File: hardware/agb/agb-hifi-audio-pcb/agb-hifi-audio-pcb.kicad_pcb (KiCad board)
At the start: 4 copper layers, 28.5 x 35.1 mm, 72 parts, among them J1 TC2030-IDC-NL, J5 SPK+, J6 SPK-, J7 EXPANSION0, J8 EXPANSION1, U1 ESP32-PICO-MINI-02-N8R2, U2 ES8388, U3 TPS61021ADSGR, U4 PAM8302AASCR, U5 LP5907MFX-3.0

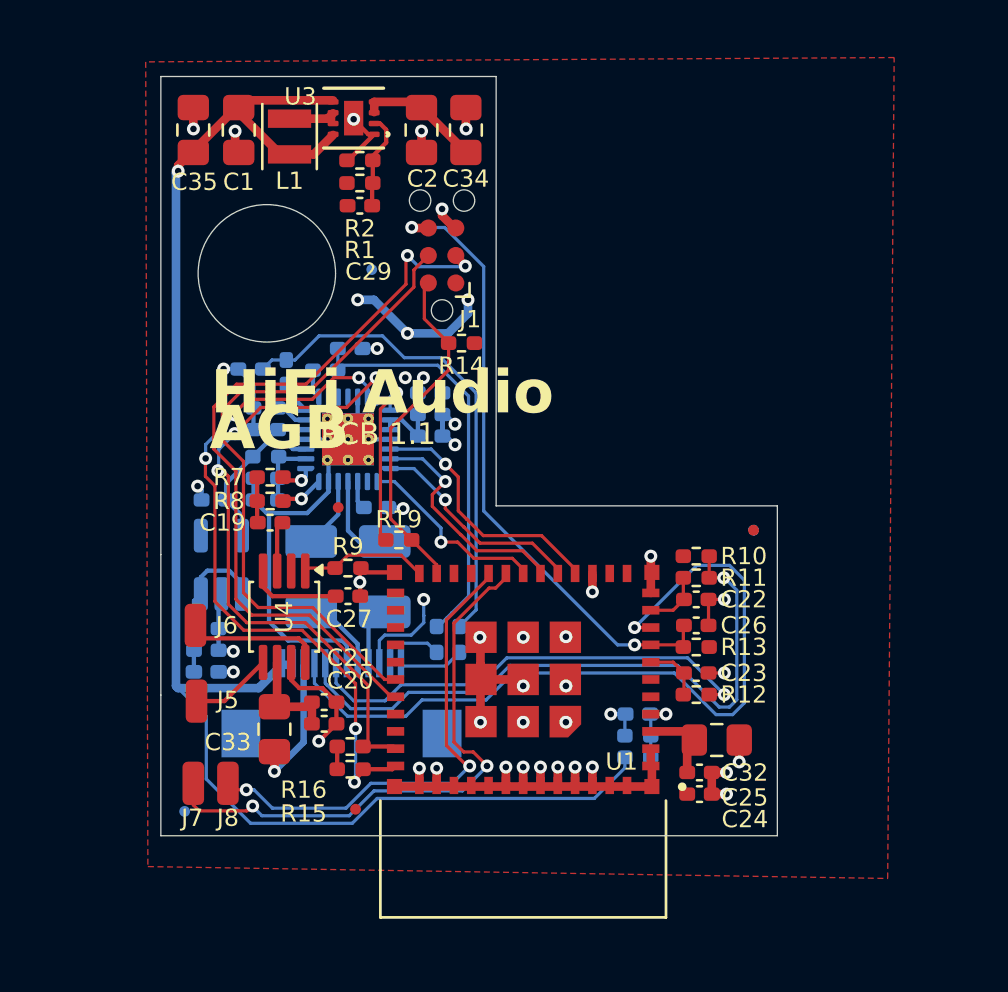
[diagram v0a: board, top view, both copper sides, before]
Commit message: hardware(agb): reroute mod PCB for the smaller shell fit; trim + reinforce FPC lead
Mod PCB: full reroute after narrowing the outline 28.5mm -> 25.35mm to fit the
shell. U2 (codec) moved and rotated 90deg with NT1 following; fiducials dropped
(sub-70x70 boards ride JLCPCB rails, which carry their own). Layout review
verified clean: DRC 0 unconnected, antenna keep-outs intact with the module
antenna overhanging the edge, zones refilled, power widths unchanged.

FPC: lead tip trimmed 1.25mm (y128 -> y126.75) to clear the volume wheel --
1.6mm is the geometric max without moving the J5 finger pattern, and the
shorter setback lands closer to the Hirose copper-to-tip recommendation.
Stiffener pulled flush with the new tip (4.85mm coverage vs 4.5mm minimum).
R2.0 fillets on both lead-base corners so the base stops tearing. Per-pad
0.15mm clearance overrides on the 12-pos connector pads.
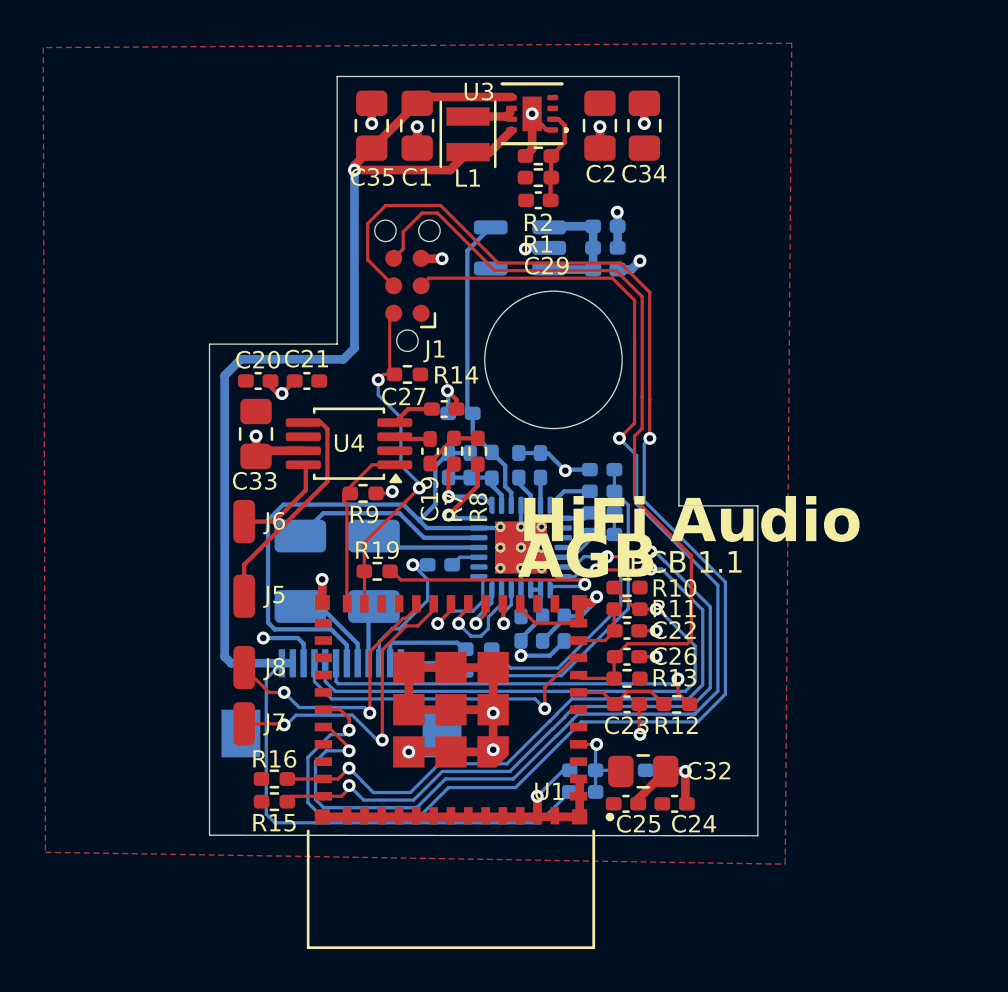
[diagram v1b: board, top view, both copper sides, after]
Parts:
- removed FID4 (x5), FID6: Fiducial_0.5mm_Mask1mm, Fiducial:Fiducial_0.5mm_Mask1mm
- moved C6 26.2 mm to (109.2, 98.2)
- moved C7 26.2 mm to (109.2, 99.2)
- moved FB1 26.2 mm to (109.2, 100.2)
- moved U5 20.1 mm to (105.2, 99.2), turned to 180 degrees
- moved C13 16.9 mm to (109.0, 109.5)
- moved C20 16.1 mm to (93.2, 105.4)
- moved C15 15.6 mm to (109.0, 110.5), turned to 180 degrees
- moved C21 14.9 mm to (95.4, 105.4), turned to 180 degrees
- moved C14 14.5 mm to (109.0, 112.5), turned to 180 degrees
- moved C16 14.4 mm to (109.0, 111.5)
- moved C33 13.7 mm to (93.0, 107.8)
- moved C12 13.0 mm to (106.2, 109.3), turned to 90 degrees
- moved C5 12.5 mm to (107.3, 116.8), turned to 90 degrees
- moved C31 12.1 mm to (102.5, 106.9)
- moved C11 11.8 mm to (105.2, 109.3), turned to 90 degrees
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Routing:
- net UART_RX: track 30.5 -> 66.9 mm, vias 0 -> 2
- net UART_TX: track 34.5 -> 56.7 mm
- net PAIR: track 36.2 -> 14.9 mm
- net +3V3: track 26.7 -> 7.27 mm, vias 5 -> 2
- net EXP0: track 26.8 -> 14.4 mm
- net EXP1: track 22.1 -> 12.5 mm
- net ESP_EN: track 28.8 -> 38.1 mm, vias 2 -> 0
- net AGND: track 15.6 -> 24.8 mm
- net I2S_BCLK: track 11.8 -> 2.64 mm
- net Net-(C13-Pad1): track 22.7 -> 14.1 mm
- net GND: track 82.0 -> 90.4 mm, vias 42 -> 25
- net I2S_LRCK: track 9.90 -> 2.97 mm
- net AVDD: track 7.28 -> 14.1 mm
- net Net-(C14-Pad1): track 18.6 -> 11.9 mm
- net SPK+: track 4.14 -> 10.6 mm
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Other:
- board size 28.5 x 35.1 mm -> 25.3 x 35.1 mm
